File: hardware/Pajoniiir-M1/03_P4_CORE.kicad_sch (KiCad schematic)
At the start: 42 parts, among them U1 ESP32-P4NRW32X, U3 TLV62569DRLR

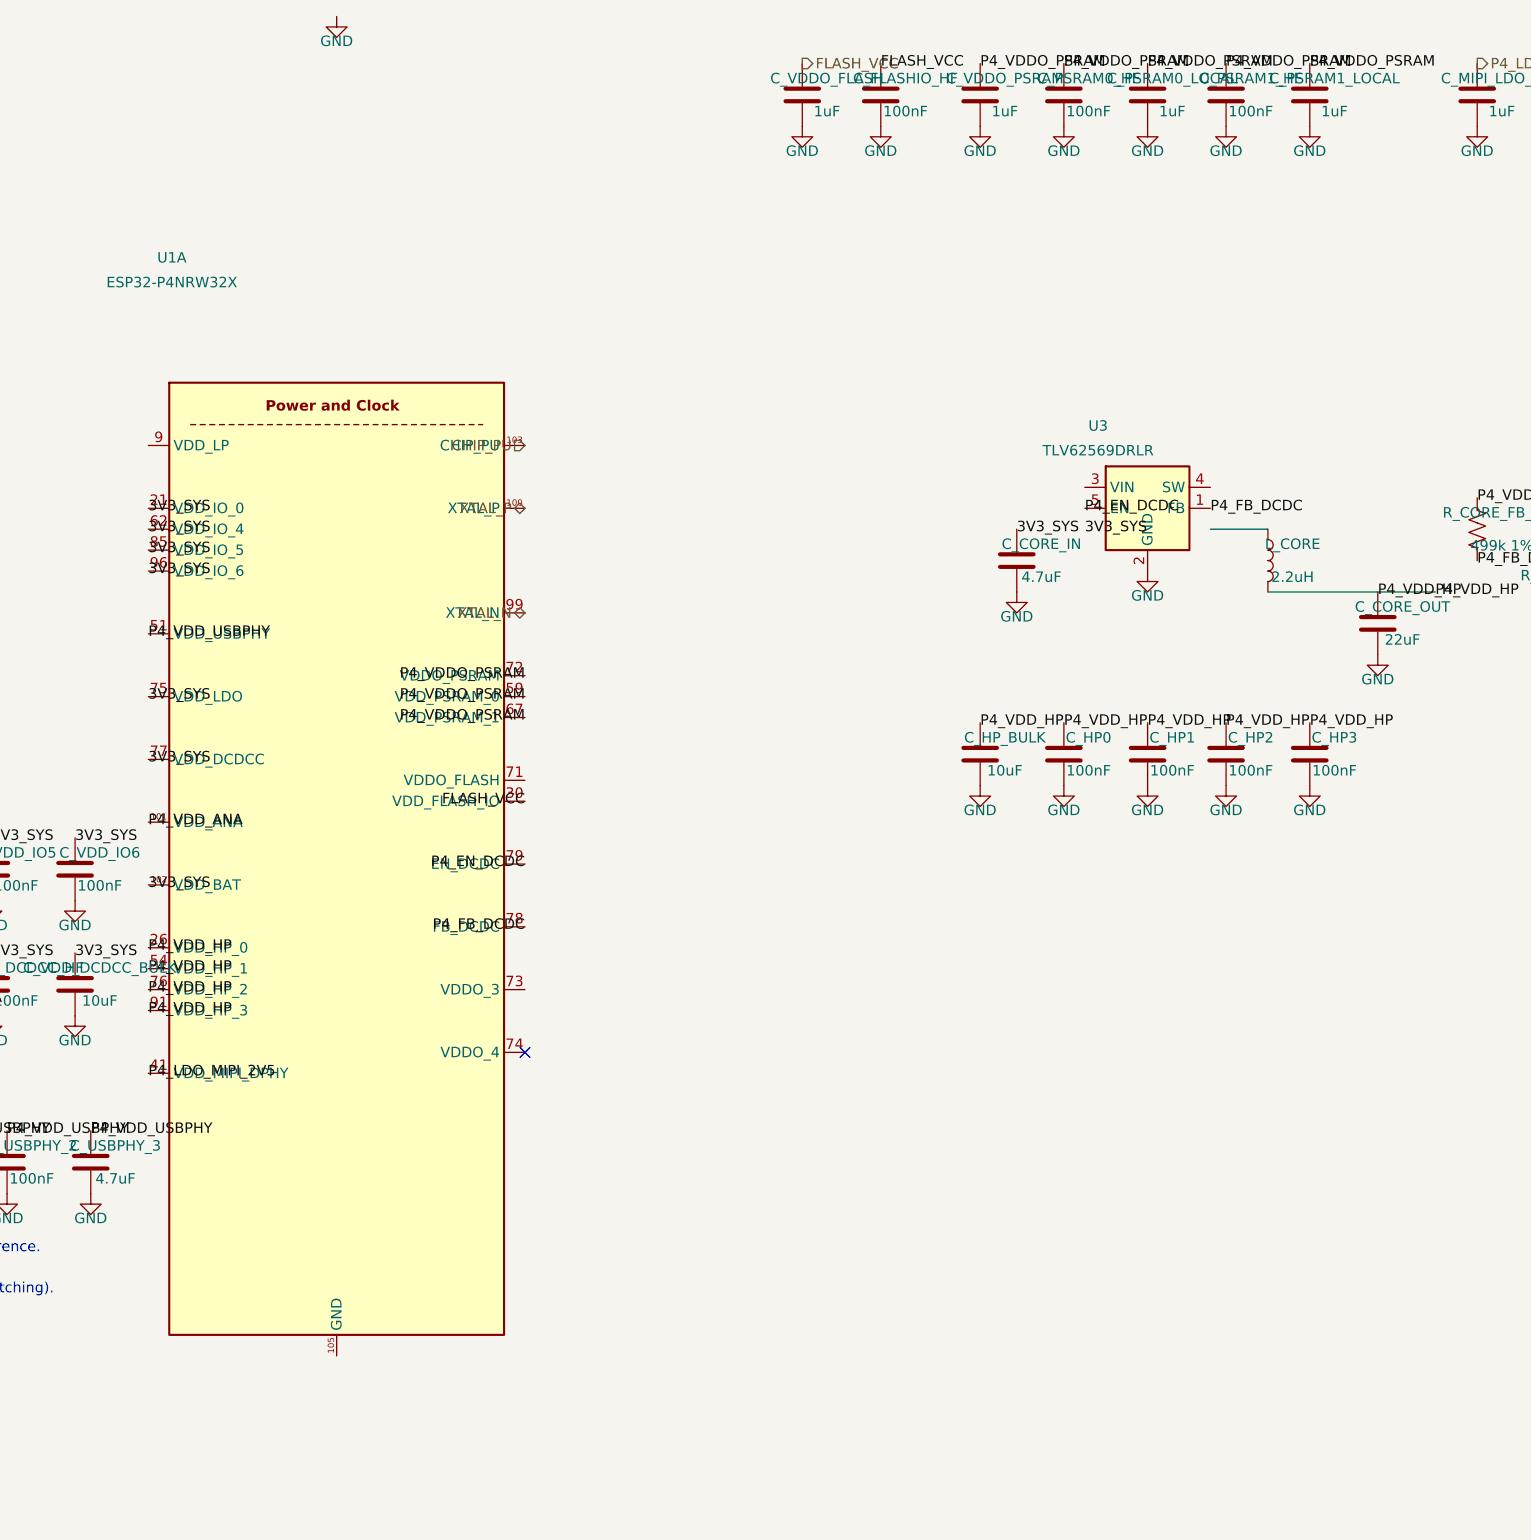
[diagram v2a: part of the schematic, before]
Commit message: hardware: repair P4 power endpoints and core buck routing
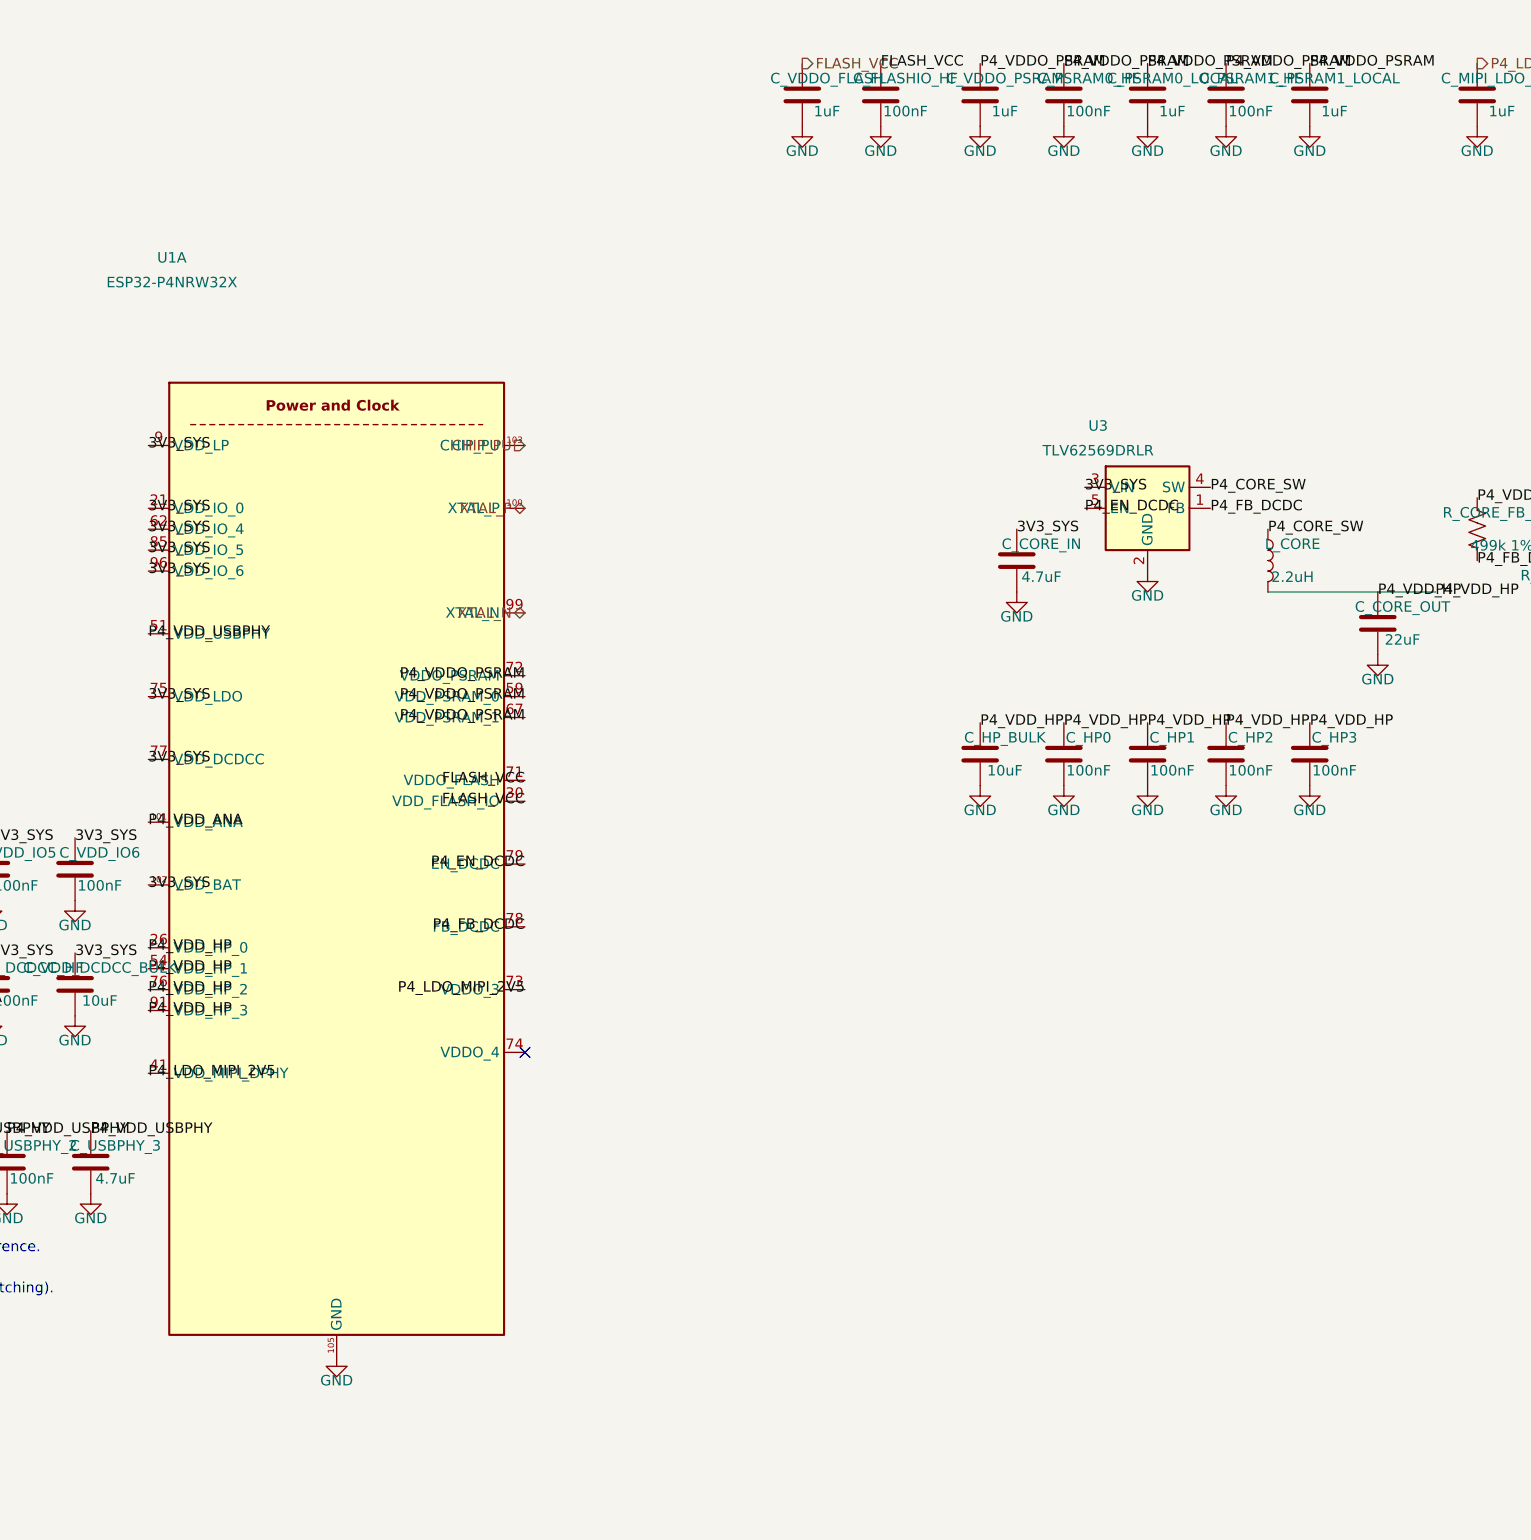
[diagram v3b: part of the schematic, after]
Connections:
- net 3V3_SYS: now also U1.9 (VDD_LP), U3.3 (VIN)
- net FLASH_VCC: now also U1.71 (VDDO_FLASH)
- net GND: now also U1.105 (GND)
- net P4_LDO_MIPI_2V5: now also U1.73 (VDDO_3)
- net P4_CORE_SW: now reaches U3.4 (SW)
- net P4_CORE_SW: now also L_CORE.1
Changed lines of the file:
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@@
   (label "DSI_REXT" (at 301.625 269.875 180) (effects (font (size 1.27 1.27))))
   (label "DSI_REXT" (at 307.34 160.02 0) (effects (font (size 1.27 1.27))))
+  (label "3V3_SYS" (at 88.9 82.55 0) (effects (font (size 1.27 1.27))))
   (symbol
     (lib_id "Pajoniiir-M1:ESP32-P4X")
@@
     (instances (project "Pajoniiir-M1" (path "/2c8dd352-b7b8-4d9e-8f93-5dd43be2a100/31000003-6b2a-4a3a-8c91-000000000003" (reference "#PWR0392") (unit 1))))
   )
+  (label "FLASH_VCC" (at 134.62 123.19 180) (effects (font (size 1.27 1.27))))
   (label "FLASH_VCC" (at 134.62 125.73 180) (effects (font (size 1.27 1.27))))
   (hierarchical_label "FLASH_VCC" (shape output) (at 168.275 36.195 0) (effects (font (size 1.27 1.27))))
@@
   )
   (label "P4_LDO_MIPI_2V5" (at 88.9 158.75 0) (effects (font (size 1.27 1.27))))
+  (label "P4_LDO_MIPI_2V5" (at 134.62 148.59 180) (effects (font (size 1.27 1.27))))
   (hierarchical_label "P4_LDO_MIPI_2V5" (shape output) (at 250.19 36.195 0) (effects (font (size 1.27 1.27))))
   (symbol
@@
   (no_connect (at 134.62 156.21))
   (symbol
-    (lib_id "power:GND") (at 111.76 30.48 0) (unit 1)
-    (exclude_from_sim no) (in_bom yes) (on_board yes) (dnp no)
-    (property "Reference" "#PWR0303" (at 111.76 36.48 0) (effects (font (size 1.27 1.27)) (hide yes)))
-    (property "Value" "GND" (at 111.76 33.48 0) (effects (font (size 1.27 1.27))))
-    (property "Footprint" "" (at 111.76 30.48 0) (effects (font (size 1.27 1.27)) (hide yes)))
-    (property "Datasheet" "" (at 111.76 30.48 0) (effects (font (size 1.27 1.27)) (hide yes)))
+    (lib_id "power:GND") (at 111.76 193.04 0) (unit 1)
+    (exclude_from_sim no) (in_bom yes) (on_board yes) (dnp no)
+    (property "Reference" "#PWR0303" (at 111.76 199.04 0) (effects (font (size 1.27 1.27)) (hide yes)))
+    (property "Value" "GND" (at 111.76 196.04 0) (effects (font (size 1.27 1.27))))
+    (property "Footprint" "" (at 111.76 193.04 0) (effects (font (size 1.27 1.27)) (hide yes)))
+    (property "Datasheet" "" (at 111.76 193.04 0) (effects (font (size 1.27 1.27)) (hide yes)))
     (pin "1")
     (instances (project "Pajoniiir-M1" (path "/2c8dd352-b7b8-4d9e-8f93-5dd43be2a100/31000003-6b2a-4a3a-8c91-000000000003" (reference "#PWR0303") (unit 1))))
@@
     (instances (project "Pajoniiir-M1" (path "/2c8dd352-b7b8-4d9e-8f93-5dd43be2a100/31000003-6b2a-4a3a-8c91-000000000003" (reference "U3") (unit 1))))
   )
-  (label "3V3_SYS" (at 202.565 92.71 0) (effects (font (size 1.27 1.27))))
+  (label "3V3_SYS" (at 202.565 87.63 0) (effects (font (size 1.27 1.27))))
   (symbol
     (lib_id "Device:C") (at 194.31 96.52 0) (unit 1)
@@
     (instances (project "Pajoniiir-M1" (path "/2c8dd352-b7b8-4d9e-8f93-5dd43be2a100/31000003-6b2a-4a3a-8c91-000000000003" (reference "#PWR0305") (unit 1))))
   )
-  (wire (pts (xy 217.805 92.71) (xy 224.79 92.71)) (stroke (width 0) (type default)))
+  (label "P4_CORE_SW" (at 217.805 87.63 0) (effects (font (size 1.27 1.27))))
+  (label "P4_CORE_SW" (at 224.79 92.71 0) (effects (font (size 1.27 1.27))))
   (symbol
     (lib_id "Device:L") (at 224.79 96.52 0) (unit 1)

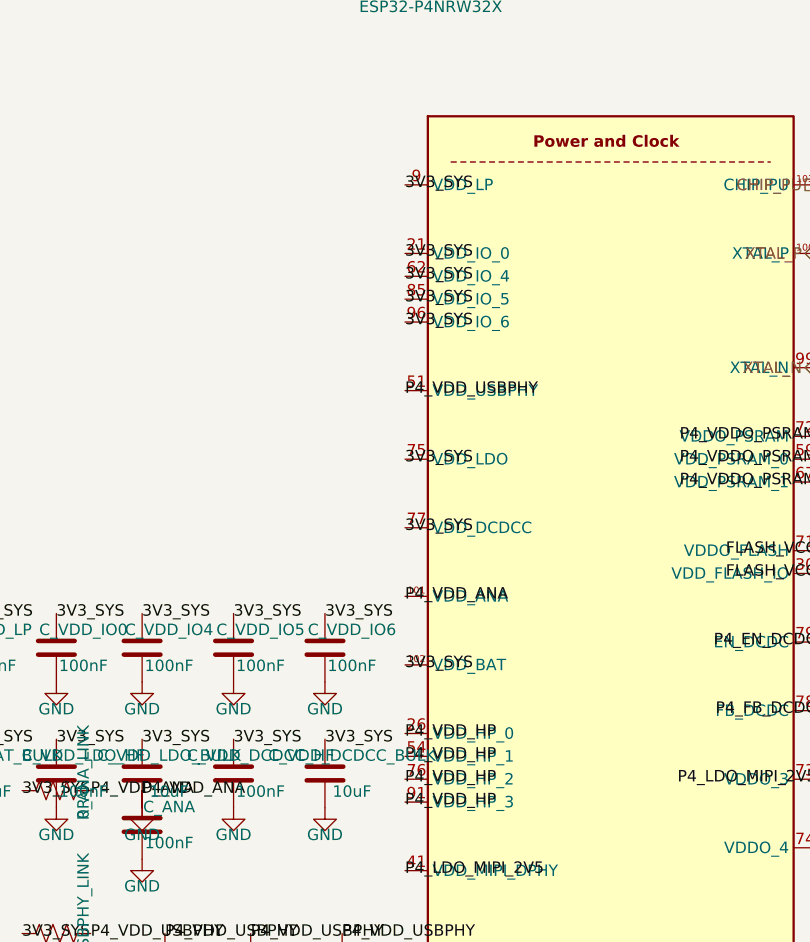
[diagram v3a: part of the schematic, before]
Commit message: hardware: declare verified rail power sources for ERC
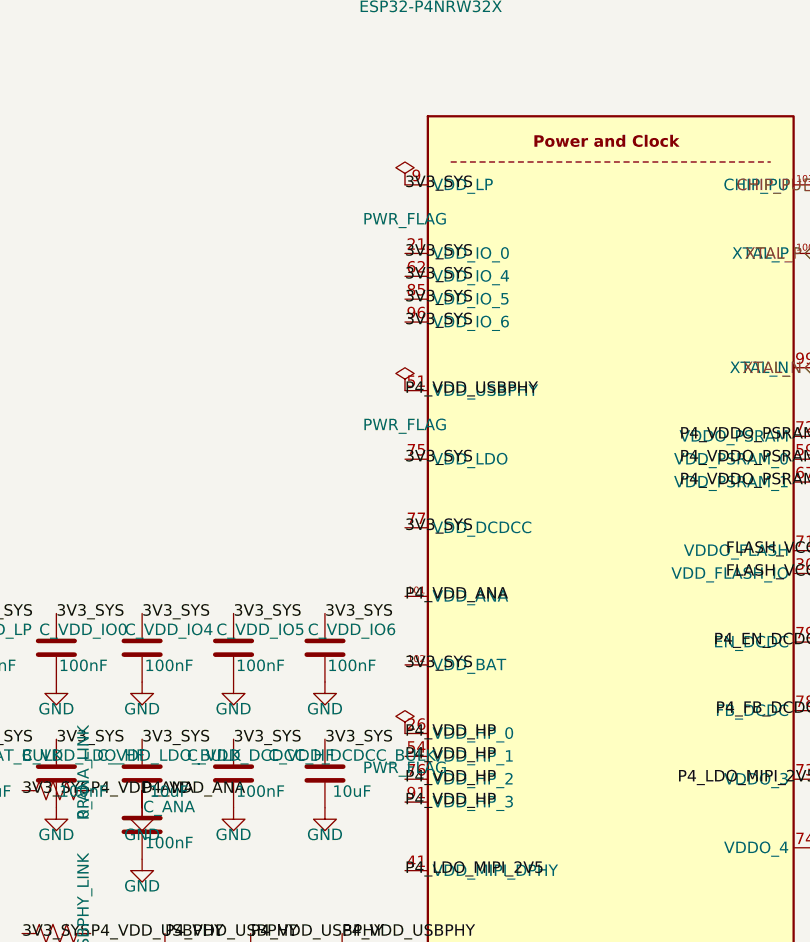
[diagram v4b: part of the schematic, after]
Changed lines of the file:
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@@
   (text "VDDO_3 is firmware-configured to 2.5V for MIPI DPHY. VDDO_4 is intentionally unused/NC in Rev A (no SDIO 3.0 voltage switching)." (exclude_from_sim no) (at 20 185 0) (effects (font (size 1.27 1.27))))
   (text "ESP32-P4NRW32X requires a separate v3.x firmware build; legacy JC4880 rev1.3 binary is not valid for M1." (exclude_from_sim no) (at 20 190 0) (effects (font (size 1.27 1.27))))
+  (symbol
+    (lib_id "power:PWR_FLAG")
+    (at 88.9 82.55 0)
+    (unit 1)
+    (exclude_from_sim no)
+    (in_bom yes)
+    (on_board yes)
+    (dnp no)
+    (property "Reference" "#FLG0301" (at 88.9 84.455 0) (effects (font (size 1.27 1.27)) (hide yes)))
+    (property "Value" "PWR_FLAG" (at 88.9 86.36 0) (effects (font (size 1.27 1.27))))
+    (property "Footprint" "" (at 88.9 82.55 0) (effects (font (size 1.27 1.27)) (hide yes)))
+    (property "Datasheet" "~" (at 88.9 82.55 0) (effects (font (size 1.27 1.27)) (hide yes)))
+    (property "Description" "Special symbol for telling ERC where power comes from" (at 88.9 82.55 0) (effects (font (size 1.27 1.27)) (hide yes)))
+    (pin "1")
+    (instances (project "Pajoniiir-M1" (path "/2c8dd352-b7b8-4d9e-8f93-5dd43be2a100/31000003-6b2a-4a3a-8c91-000000000003" (reference "#FLG0301") (unit 1))))
+  )
+  (symbol
+    (lib_id "power:PWR_FLAG")
+    (at 88.9 105.41 0)
+    (unit 1)
+    (exclude_from_sim no)
+    (in_bom yes)
+    (on_board yes)
+    (dnp no)
+    (property "Reference" "#FLG0302" (at 88.9 107.315 0) (effects (font (size 1.27 1.27)) (hide yes)))
+    (property "Value" "PWR_FLAG" (at 88.9 109.22 0) (effects (font (size 1.27 1.27))))
+    (property "Footprint" "" (at 88.9 105.41 0) (effects (font (size 1.27 1.27)) (hide yes)))
+    (property "Datasheet" "~" (at 88.9 105.41 0) (effects (font (size 1.27 1.27)) (hide yes)))
+    (property "Description" "Special symbol for telling ERC where power comes from" (at 88.9 105.41 0) (effects (font (size 1.27 1.27)) (hide yes)))
+    (pin "1")
+    (instances (project "Pajoniiir-M1" (path "/2c8dd352-b7b8-4d9e-8f93-5dd43be2a100/31000003-6b2a-4a3a-8c91-000000000003" (reference "#FLG0302") (unit 1))))
+  )
+  (symbol
+    (lib_id "power:PWR_FLAG")
+    (at 88.9 143.51 0)
+    (unit 1)
+    (exclude_from_sim no)
+    (in_bom yes)
+    (on_board yes)
+    (dnp no)
+    (property "Reference" "#FLG0303" (at 88.9 145.415 0) (effects (font (size 1.27 1.27)) (hide yes)))
+    (property "Value" "PWR_FLAG" (at 88.9 147.32 0) (effects (font (size 1.27 1.27))))
+    (property "Footprint" "" (at 88.9 143.51 0) (effects (font (size 1.27 1.27)) (hide yes)))
+    (property "Datasheet" "~" (at 88.9 143.51 0) (effects (font (size 1.27 1.27)) (hide yes)))
+    (property "Description" "Special symbol for telling ERC where power comes from" (at 88.9 143.51 0) (effects (font (size 1.27 1.27)) (hide yes)))
+    (pin "1")
+    (instances (project "Pajoniiir-M1" (path "/2c8dd352-b7b8-4d9e-8f93-5dd43be2a100/31000003-6b2a-4a3a-8c91-000000000003" (reference "#FLG0303") (unit 1))))
+  )
   (sheet_instances (path "/" (page "4")))
   (embedded_fonts no)
